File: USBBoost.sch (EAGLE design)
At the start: 27 parts, among them IC1 RT9276, J1 Input, J2 3.75V, J3 2.33V, J4 1.17V, J5 Status, X1 USB_

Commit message: foo
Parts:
- removed R15: 20k0, freetronics-original:RESISTOR0603
- added R3: 49k9, freetronics-original:RESISTOR0603
- R10: value 1k -> 130k
- R11: value 130k -> 73k2
- R12: value 73k2 -> 26k7
- R13: value 26k7 -> 20k
- R14: value 20k -> 20k0
- R5: value 49k9 -> 180k
- R6: value 180k -> 10k
- R8: value 10k -> 1k
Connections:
- net !LBO: now also R7.2; no longer R8.2
- net !PGOOD: now also R6.2; no longer R7.2
- net FB: now also R14.2, R5.2; no longer R15.2, R6.2
- net GND: now also R13.1, R3.2; no longer R15.1, R5.2
- net LBI: now also R10.1, R13.2; no longer R13.1, R14.2
- net N$10: now also R4.1; no longer R5.1
- net N$11: now also R11.2; no longer R12.2
- net N$12: now also R12.2; no longer R13.2
- net N$15: now also R9.2; no longer R10.2
- net N$5: now also R10.2; no longer R11.2
- net N$7: now also R3.1; no longer R4.1
- net N$8: now also R8.2; no longer R9.2
- net VOUT: now also R5.1; no longer R10.1
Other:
- note added: "Jumpers J2, J3 and J4 change the input voltage to the internal low-battery comparator output."
- note added: "or 1 or 2x alkaline (1.5V) or NiMH (1.2V) cells."
- note removed: "or 2 x alkaline or NiMH"
- moved on the sheet: R10, R11, R12, R13, R14, R4, R5, R6, R7, R8, R9

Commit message: foo
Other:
- note added: "L1: Same inductor as EtherMega SMPS."
- note removed: "Inductor - same device as used on EtherMega."
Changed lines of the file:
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@@
 <setting verticaltext="up"/>
 </settings>
-<grid distance="0.1" unitdist="inch" unit="inch" style="lines" multiple="1" display="yes" altdistance="0.01" altunitdist="inch" altunit="inch"/>
+<grid distance="0.1" unitdist="inch" unit="inch" style="lines" multiple="1" display="no" altdistance="0.01" altunitdist="inch" altunit="inch"/>
 <layers>
-<layer number="1" name="Top" color="4" fill="1" visible="no" active="no"/>
-<layer number="2" name="Route2" color="1" fill="3" visible="no" active="no"/>
-<layer number="3" name="Route3" color="4" fill="3" visible="no" active="no"/>
-<layer number="4" name="Route4" color="1" fill="4" visible="no" active="no"/>
-<layer number="5" name="Route5" color="4" fill="4" visible="no" active="no"/>
-<layer number="6" name="Route6" color="1" fill="8" visible="no" active="no"/>
-<layer number="7" name="Route7" color="4" fill="8" visible="no" active="no"/>
-<layer number="8" name="Route8" color="1" fill="2" visible="no" active="no"/>
-<layer number="9" name="Route9" color="4" fill="2" visible="no" active="no"/>
-<layer number="10" name="Route10" color="1" fill="7" visible="no" active="no"/>
-<layer number="11" name="Route11" color="4" fill="7" visible="no" active="no"/>
-<layer number="12" name="Route12" color="1" fill="5" visible="no" active="no"/>
-<layer number="13" name="Route13" color="4" fill="5" visible="no" active="no"/>
-<layer number="14" name="Route14" color="1" fill="6" visible="no" active="no"/>
-<layer number="15" name="Route15" color="4" fill="6" visible="no" active="no"/>
-<layer number="16" name="Bottom" color="1" fill="1" visible="no" active="no"/>
-<layer number="17" name="Pads" color="2" fill="1" visible="no" active="no"/>
-<layer number="18" name="Vias" color="2" fill="1" visible="no" active="no"/>
-<layer number="19" name="Unrouted" color="14" fill="1" visible="no" active="no"/>
-<layer number="20" name="Dimension" color="15" fill="1" visible="no" active="no"/>
-<layer number="21" name="tPlace" color="16" fill="1" visible="no" active="no"/>
-<layer number="22" name="bPlace" color="14" fill="1" visible="no" active="no"/>
-<layer number="23" name="tOrigins" color="15" fill="1" visible="no" active="no"/>
-<layer number="24" name="bOrigins" color="15" fill="1" visible="no" active="no"/>
-<layer number="25" name="tNames" color="7" fill="1" visible="no" active="no"/>
-<layer number="26" name="bNames" color="7" fill="1" visible="no" active="no"/>
-<layer number="27" name="tValues" color="7" fill="1" visible="no" active="no"/>
-<layer number="28" name="bValues" color="7" fill="1" visible="no" active="no"/>
+<layer number="1" name="Top" color="4" fill="1" visible="yes" active="no"/>
+<layer number="2" name="Route2" color="1" fill="3" visible="yes" active="no"/>
+<layer number="3" name="Route3" color="4" fill="3" visible="yes" active="no"/>
+<layer number="4" name="Route4" color="1" fill="4" visible="yes" active="no"/>
+<layer number="5" name="Route5" color="4" fill="4" visible="yes" active="no"/>
+<layer number="6" name="Route6" color="1" fill="8" visible="yes" active="no"/>
+<layer number="7" name="Route7" color="4" fill="8" visible="yes" active="no"/>
+<layer number="8" name="Route8" color="1" fill="2" visible="yes" active="no"/>
+<layer number="9" name="Route9" color="4" fill="2" visible="yes" active="no"/>
+<layer number="10" name="Route10" color="1" fill="7" visible="yes" active="no"/>
+<layer number="11" name="Route11" color="4" fill="7" visible="yes" active="no"/>
+<layer number="12" name="Route12" color="1" fill="5" visible="yes" active="no"/>
+<layer number="13" name="Route13" color="4" fill="5" visible="yes" active="no"/>
+<layer number="14" name="Route14" color="1" fill="6" visible="yes" active="no"/>
+<layer number="15" name="Route15" color="4" fill="6" visible="yes" active="no"/>
+<layer number="16" name="Bottom" color="1" fill="1" visible="yes" active="no"/>
+<layer number="17" name="Pads" color="2" fill="1" visible="yes" active="no"/>
+<layer number="18" name="Vias" color="2" fill="1" visible="yes" active="no"/>
+<layer number="19" name="Unrouted" color="14" fill="1" visible="yes" active="no"/>
+<layer number="20" name="Dimension" color="15" fill="1" visible="yes" active="no"/>
+<layer number="21" name="tPlace" color="16" fill="1" visible="yes" active="no"/>
+<layer number="22" name="bPlace" color="14" fill="1" visible="yes" active="no"/>
+<layer number="23" name="tOrigins" color="15" fill="1" visible="yes" active="no"/>
+<layer number="24" name="bOrigins" color="15" fill="1" visible="yes" active="no"/>
+<layer number="25" name="tNames" color="7" fill="1" visible="yes" active="no"/>
+<layer number="26" name="bNames" color="7" fill="1" visible="yes" active="no"/>
+<layer number="27" name="tValues" color="7" fill="1" visible="yes" active="no"/>
+<layer number="28" name="bValues" color="7" fill="1" visible="yes" active="no"/>
 <layer number="29" name="tStop" color="7" fill="3" visible="no" active="no"/>
 <layer number="30" name="bStop" color="7" fill="6" visible="no" active="no"/>
@@
 <layer number="35" name="tGlue" color="7" fill="4" visible="no" active="no"/>
 <layer number="36" name="bGlue" color="7" fill="5" visible="no" active="no"/>
-<layer number="37" name="tTest" color="7" fill="1" visible="no" active="no"/>
-<layer number="38" name="bTest" color="7" fill="1" visible="no" active="no"/>
+<layer number="37" name="tTest" color="7" fill="1" visible="yes" active="no"/>
+<layer number="38" name="bTest" color="7" fill="1" visible="yes" active="no"/>
 <layer number="39" name="tKeepout" color="4" fill="11" visible="no" active="no"/>
 <layer number="40" name="bKeepout" color="1" fill="11" visible="no" active="no"/>
@@
 <layer number="44" name="Drills" color="7" fill="1" visible="no" active="no"/>
 <layer number="45" name="Holes" color="7" fill="1" visible="no" active="no"/>
-<layer number="46" name="Milling" color="3" fill="1" visible="no" active="no"/>
-<layer number="47" name="Measures" color="7" fill="1" visible="no" active="no"/>
-<layer number="48" name="Document" color="7" fill="1" visible="no" active="no"/>
-<layer number="49" name="Reference" color="7" fill="1" visible="no" active="no"/>
-<layer number="50" name="dxf" color="7" fill="1" visible="no" active="no"/>
-<layer number="51" name="tDocu" color="6" fill="1" visible="no" active="no"/>
-<layer number="52" name="bDocu" color="7" fill="1" visible="no" active="no"/>
-<layer number="53" name="tGND_GNDA" color="7" fill="9" visible="no" active="no"/>
-<layer number="54" name="bGND_GNDA" color="1" fill="9" visible="no" active="no"/>
-<layer number="56" name="wert" color="7" fill="1" visible="no" active="no"/>
+<layer number="46" name="Milling" color="3" fill="1" visible="yes" active="no"/>
+<layer number="47" name="Measures" color="7" fill="1" visible="yes" active="no"/>
+<layer number="48" name="Document" color="7" fill="1" visible="yes" active="no"/>
+<layer number="49" name="Reference" color="7" fill="1" visible="yes" active="no"/>
+<layer number="50" name="dxf" color="7" fill="1" visible="yes" active="no"/>
+<layer number="51" name="tDocu" color="6" fill="1" visible="yes" active="no"/>
+<layer number="52" name="bDocu" color="7" fill="1" visible="yes" active="no"/>
+<layer number="53" name="tGND_GNDA" color="7" fill="9" visible="yes" active="no"/>
+<layer number="54" name="bGND_GNDA" color="1" fill="9" visible="yes" active="no"/>
+<layer number="56" name="wert" color="7" fill="1" visible="yes" active="no"/>
 <layer number="91" name="Nets" color="2" fill="1" visible="yes" active="yes"/>
 <layer number="92" name="Busses" color="1" fill="1" visible="yes" active="yes"/>
@@
 <plain>
 <text x="205.74" y="101.6" size="1.4224" layer="98">Vout = 5.0V</text>
-<text x="30.48" y="111.76" size="1.27" layer="98">or 1 or 2x alkaline (1.5V) or NiMH (1.2V) cells.</text>
-<text x="30.48" y="114.3" size="1.27" layer="98">eg. single-cell Li-ion battery</text>
+<text x="30.48" y="116.84" size="1.27" layer="98">or 1 or 2x alkaline (1.5V) or NiMH (1.2V) cells.</text>
+<text x="30.48" y="119.38" size="1.27" layer="98">eg. single-cell Li-ion battery</text>
 <text x="129.54" y="81.28" size="1.4224" layer="98">1%</text>
 <text x="129.54" y="58.42" size="1.4224" layer="98">1%</text>
@@
 <text x="193.04" y="109.22" size="1.4224" layer="98">0603</text>
 <text x="142.24" y="142.24" size="1.4224" layer="98">See http://www.ladyada.net/make/mintyboost/icharge.html</text>
-<text x="30.48" y="116.84" size="1.27" layer="98">Input voltage: 1.2 to 4.5V DC.</text>
-<text x="88.9" y="106.68" size="1.27" layer="98">CDRH</text>
+<text x="30.48" y="121.92" size="1.27" layer="98">Input voltage: 1.2 to 4.5V DC.</text>
+<text x="78.74" y="109.22" size="1.27" layer="98">CDRH</text>
 <text x="53.34" y="81.28" size="1.27" layer="98">10V</text>
 <text x="40.64" y="71.12" size="1.27" layer="98">C1: 0805 ceramic</text>
@@
 <frame x1="5.08" y1="12.7" x2="109.22" y2="25.4" columns="0" rows="0" layer="94" border-left="no" border-top="no" border-right="no" border-bottom="no"/>
 <frame x1="5.08" y1="5.08" x2="109.22" y2="17.78" columns="0" rows="0" layer="94" border-left="no" border-top="no" border-right="no" border-bottom="no"/>
-<text x="88.9" y="104.14" size="1.27" layer="98">Inductor - same device as used on EtherMega.</text>
-<text x="30.48" y="121.92" size="1.27" layer="98">Jumpers J2, J3 and J4 change the input voltage to the internal low-battery comparator output.</text>
+<text x="30.48" y="111.76" size="1.27" layer="98">L1: Same inductor as EtherMega SMPS.</text>
+<text x="30.48" y="127" size="1.27" layer="98">Jumpers J2, J3 and J4 change the input voltage to the internal low-battery comparator output.</text>
 </plain>
 <instances>

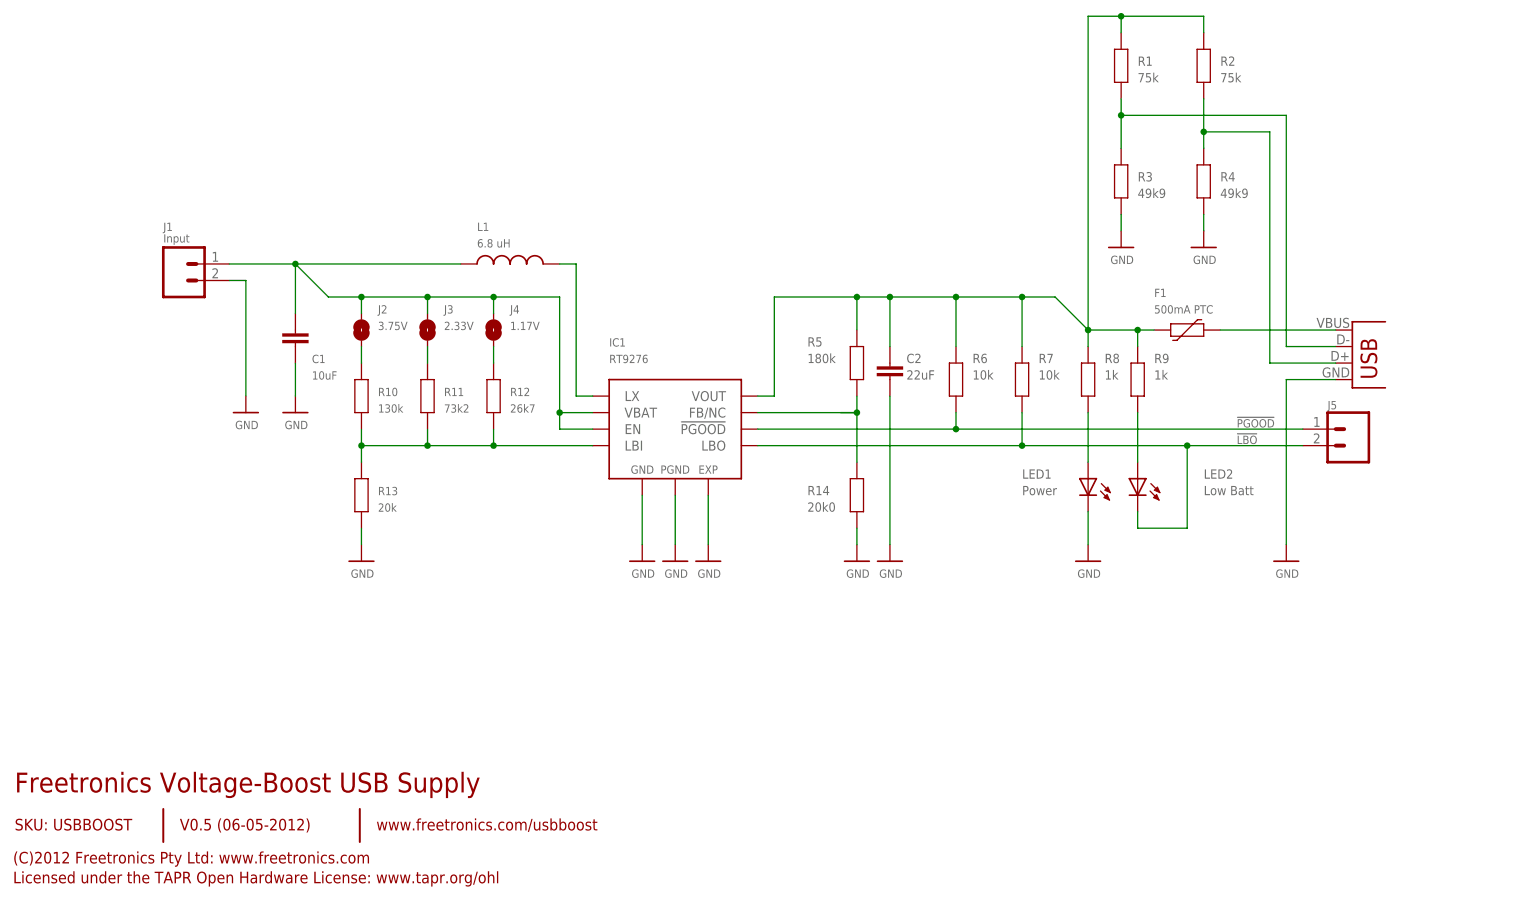
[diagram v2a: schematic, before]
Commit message: Restructured schematic
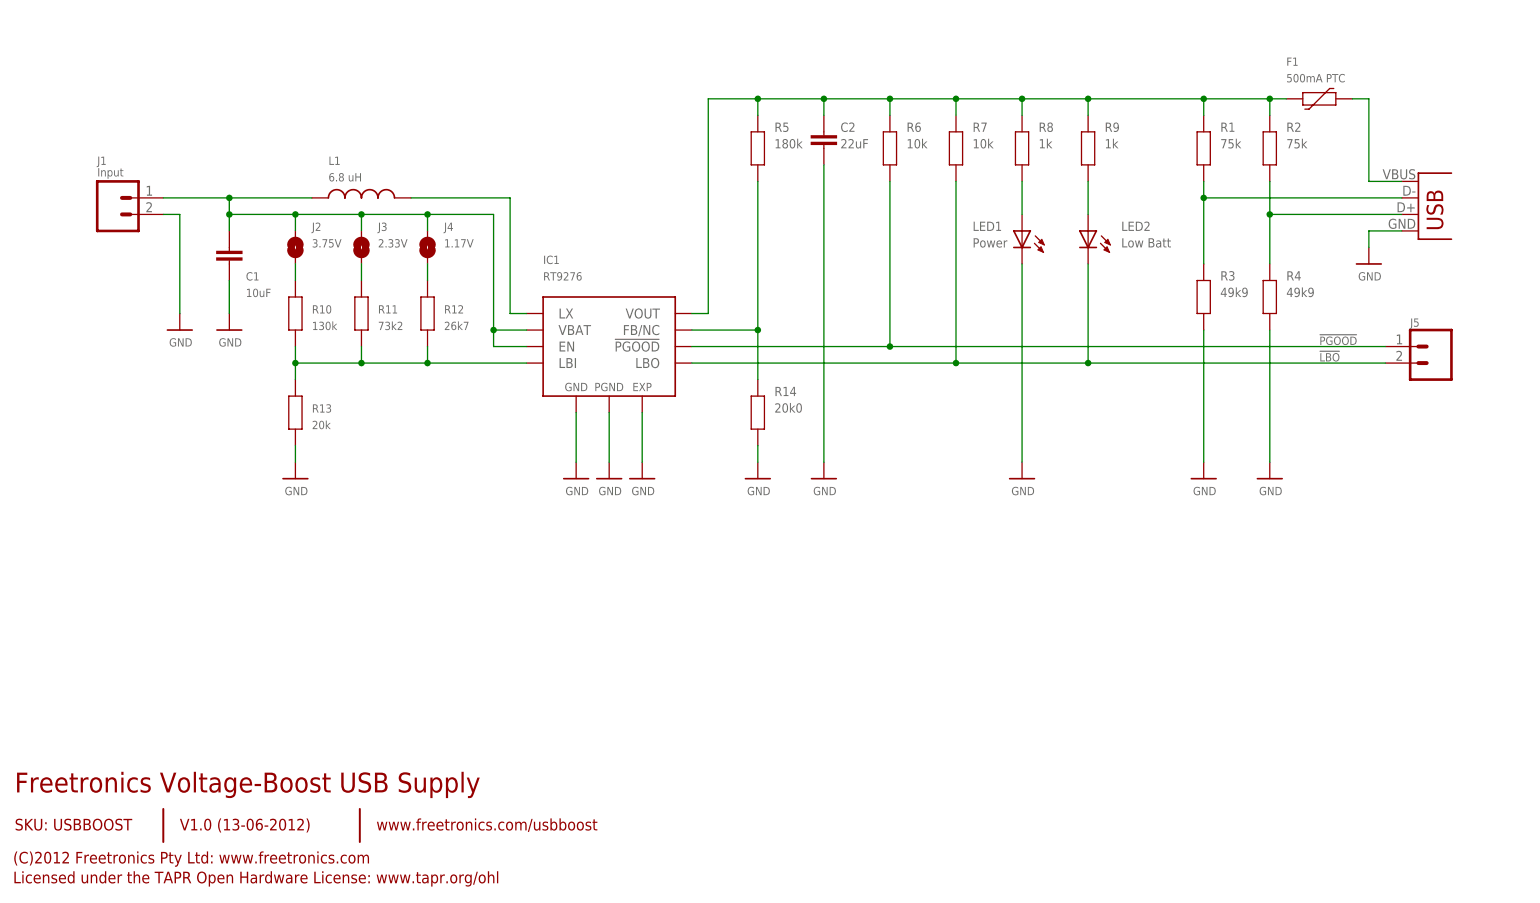
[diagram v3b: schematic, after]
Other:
- note added: "Blue"
- note added: "Red"
- note added: "V1.0 (13-06-2012)"
- note removed: "Blue 0603"
- note removed: "Red 0603"
- note removed: "V0.5 (06-05-2012)"
- moved on the sheet: C1, C2, F1, IC1, J1, J2, J3, J4, J5, L1, LED1, LED2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

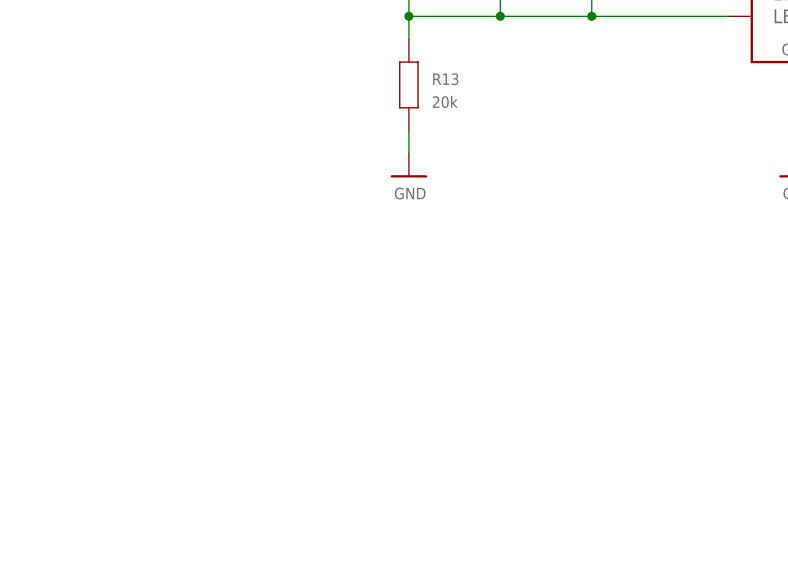
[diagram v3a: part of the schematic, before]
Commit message: Layout and schematic tweaks
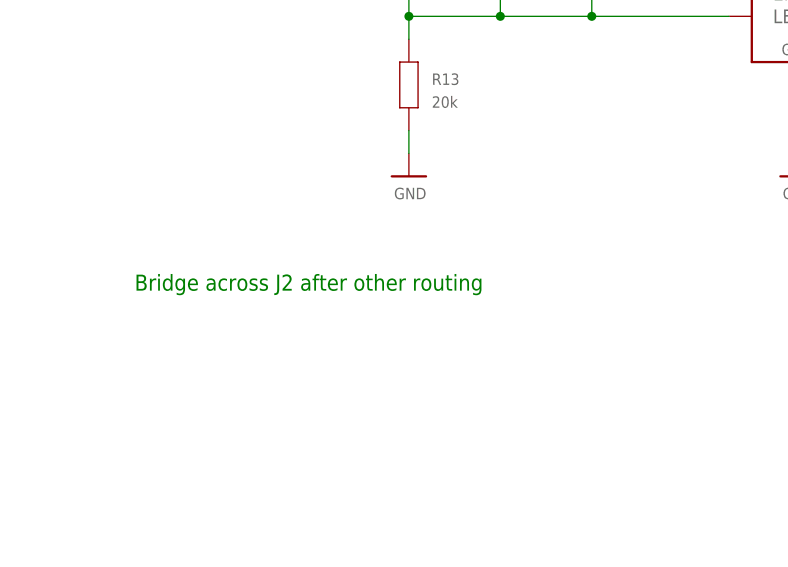
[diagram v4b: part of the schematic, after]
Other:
- note added: "Bridge across J2 after other routing"
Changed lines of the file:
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@@
 <text x="154.94" y="99.06" size="1.4224" layer="98">Blue</text>
 <text x="177.8" y="99.06" size="1.4224" layer="98">Red</text>
+<text x="20.32" y="55.88" size="1.778" layer="91">Bridge across J2 after other routing</text>
 </plain>
 <instances>

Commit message: Final tweaks and DRC for production
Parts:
- removed J1: Input, freetronics-master-v1:M02PTH
- added B1: 2P-JST-PTH, freetronics-jon:FREETRONICS-LUKE_2P-JST-TH-RAPTH
- C1: value 10uF -> 10uF ceramic
- L1: value 6.8 uH -> 7.4uH
- R1: value 75k -> 130K; device freetronics-original:RESISTOR0603 -> freetronics-master-v1.1:RESISTOR0603
- R10: value 130k -> 1K
- R11: value 73k2 -> 75K
- R12: value 26k7 -> 49K9
- R13: value 20k -> 75K
- R14: value 20k0 -> 49K9
- R2: value 75k -> 20K
- R3: value 49k9 -> 73K2
- R4: value 49k9 -> 26K7
- R5: value 180k -> 180K
- R6: value 10k -> 20K0
- R7: value 10k -> 10K
- R8: value 1k -> 10K
- R9: value 1k -> 2K2
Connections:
- net !LBO: now also R8.2; no longer R7.2
- net !PGOOD: now also R7.2; no longer R6.2
- net FB: now also R6.2; no longer R14.2
- net GND: now also B1.NEG, R12.2, R14.2, R2.1, R6.1; no longer J1.2, R13.1, R14.1, R3.2, R4.2
- net LBI: now also R1.1, R2.2, R3.1, R4.1; no longer R10.1, R11.1, R12.1, R13.2
- net N$10: now also R13.2, R14.1; no longer R2.2, R4.1
- net N$11: now also R3.2; no longer R11.2
- net N$12: now also R4.2; no longer R12.2
- net N$15: now also R10.2; no longer R9.2
- net N$5: now also R1.2; no longer R10.2
- net N$7: now also R11.2, R12.1; no longer R1.2, R3.1
- net N$8: now also R9.2; no longer R8.2
- net VBAT: now also B1.POS; no longer J1.1
- net VOUT: now also R10.1, R11.1, R13.1; no longer R1.1, R2.1, R6.1
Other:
- note added: "+"
- note added: "-"
- note added: "L1: Same inductor as EtherMega"
- note removed: "C1: 0805 ceramic"
- note removed: "L1: Same inductor as EtherMega SMPS."
- moved on the sheet: R1, R10, R11, R12, R13, R14, R2, R3, R4, R6, R7, R8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
